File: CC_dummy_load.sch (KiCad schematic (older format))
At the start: 51 parts

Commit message: improvements
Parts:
- removed C? (x3): 100n, symbol C
- removed Q?: BUK954R8-60E, symbol Q_NMOS_GDS
- removed Q?: IRF540N, TO-220, symbol IRF540N
- added C? (x2): C, symbol C
- added C? (x3): 1uF, symbol CP
- added C? (x2): 100n, symbol C
- added C?: 10uF, symbol CP
- added Q?: IRF540N, TO-220, symbol IRF540N
- added Q?: Darl_NPN, symbol Darl_NPN
- added R?: 1k, symbol R
- R?: value R -> 1k
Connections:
- wire segments 148 -> 160
- no-connect marks 3 -> 4
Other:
- note added: "Set the POT\nat 9.k\n(div /10)"
- note removed: "Set the POT\nat 9.6k\n(div /10)"
- moved on the sheet: D?, P?, RV?, U?D

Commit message: final design v1
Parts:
- added D?: D, symbol D
- added P?: CONN_01X09, symbol CONN_01X09
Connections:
- net ARDU-P05 is gone; now on net ARDU-P09: R?.2
- net ARDU-A0: now also R?.2, TH?.1, P?.1 (P1); no longer R?.1, TH?.2
- net ARDU-P08: now also P?.3 (P3)
- net ARDU-P09: now also P?.4 (P4); no longer U?.2 (~CS~)
- net ARDU-P11: now also P?.5 (P5)
- net ARDU-P13: now also P?.7 (P7)
- net GND: now also TH?.2, P?.8 (P8); no longer R?.2
- net VCC: now also R?.1, D?.2 (A); no longer TH?.1
- net ARDU-P10 renamed ARDU-P12
- net ARDU-P12: now also P?.6 (P6)
- new net: D?.1 (K), P?.9 (P9)
- new net ARDU-P07: P?.2 (P2), U?.2 (~CS~)
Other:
- note added: "ARDU-GND"
- note added: "ARDU-Vin"
- moved on the sheet: R?, TH?

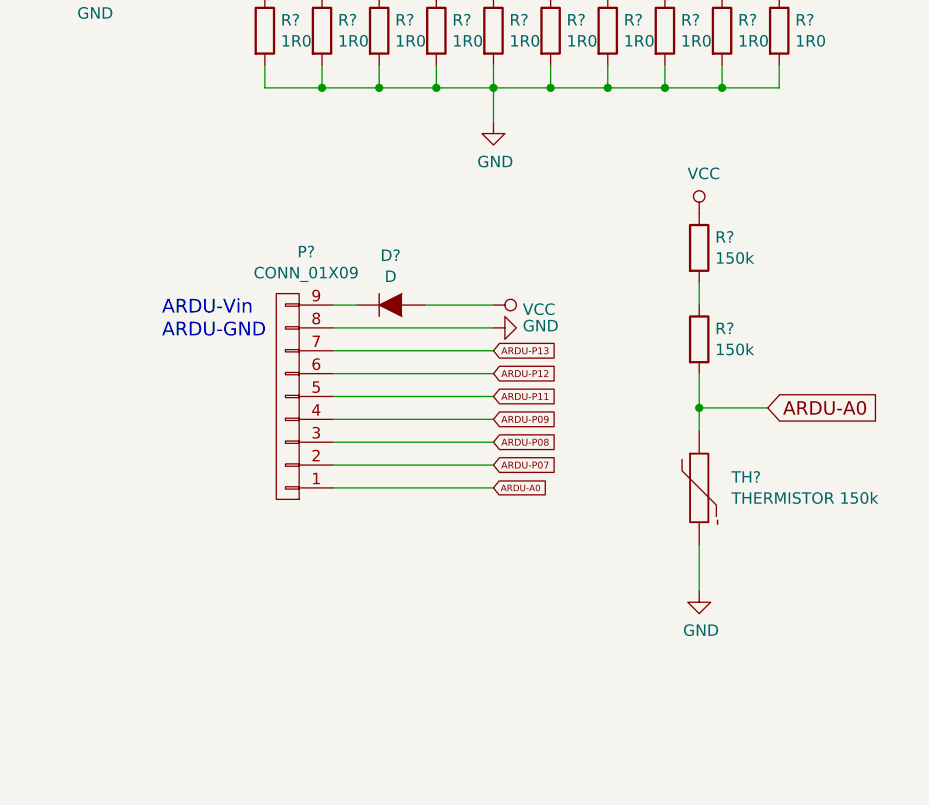
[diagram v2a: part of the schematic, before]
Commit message: change thermistor for LM35
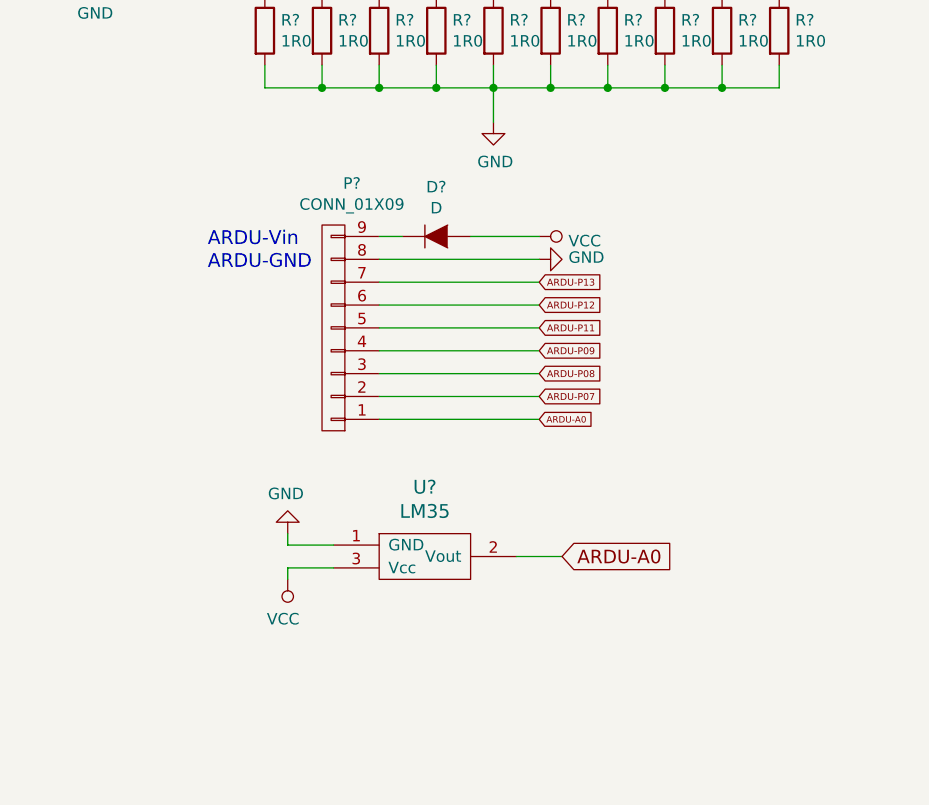
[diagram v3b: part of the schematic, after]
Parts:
- removed R? (x2): 150k, symbol R
- removed TH?: THERMISTOR 150k, symbol THERMISTOR
- added U?: LM35, symbol LM35
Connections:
- net ARDU-A0: now also U?.2 (Vout)
- net GND: now also U?.1 (GND)
- net VCC: now also U?.3 (Vcc)
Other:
- moved on the sheet: D?, P?
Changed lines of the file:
@@
 Connection ~ 6050 6450
-$Comp
-L THERMISTOR TH?
-U 1 1 56B01B45
-P 10350 5650
-F 0 "TH?" H 10491 5696 50  0000 L CNN
-F 1 "THERMISTOR 150k" H 10491 5604 50  0000 L CNN
-F 2 "" H 10350 5650 50  0000 C CNN
-F 3 "" H 10350 5650 50  0000 C CNN
-	1    10350 5650
-	1    0    0    -1
-$EndComp
 $Comp
 L VCC #PWR027
 U 1 1 56B01FB1
-P 10350 4450
-F 0 "#PWR027" H 10350 4300 50  0001 C CNN
-F 1 "VCC" H 10370 4624 50  0000 C CNN
-F 2 "" H 10350 4450 50  0000 C CNN
-F 3 "" H 10350 4450 50  0000 C CNN
-	1    10350 4450
-	1    0    0    -1
-$EndComp
-$Comp
-L R R?
-U 1 1 56B02027
-P 10350 4600
-F 0 "R?" H 10420 4646 50  0000 L CNN
-F 1 "150k" H 10420 4554 50  0000 L CNN
-F 2 "" V 10280 4600 50  0000 C CNN
-F 3 "" H 10350 4600 50  0000 C CNN
-	1    10350 4600
-	1    0    0    -1
+P 8550 6050
+F 0 "#PWR027" H 8550 5900 50  0001 C CNN
+F 1 "VCC" H 8570 6224 50  0000 C CNN
+F 2 "" H 8550 6050 50  0000 C CNN
+F 3 "" H 8550 6050 50  0000 C CNN
+	1    8550 6050
+	-1   0    0    1
 $EndComp
 $Comp
 L GND #PWR028
 U 1 1 56B020DD
-P 10350 6100
-F 0 "#PWR028" H 10350 5850 50  0001 C CNN
-F 1 "GND" H 10358 5926 50  0000 C CNN
-F 2 "" H 10350 6100 50  0000 C CNN
-F 3 "" H 10350 6100 50  0000 C CNN
-	1    10350 6100
-	1    0    0    -1
-$EndComp
-Text GLabel 10650 5300 2    59   Input ~ 0
+P 8550 5850
+F 0 "#PWR028" H 8550 5600 50  0001 C CNN
+F 1 "GND" H 8558 5676 50  0000 C CNN
+F 2 "" H 8550 5850 50  0000 C CNN
+F 3 "" H 8550 5850 50  0000 C CNN
+	1    8550 5850
+	-1   0    0    1
+$EndComp
+Text GLabel 9750 5950 2    59   Input ~ 0
 ARDU-A0
-$Comp
-L R R?
-U 1 1 56B025DE
-P 10350 5000
-F 0 "R?" H 10420 5046 50  0000 L CNN
-F 1 "150k" H 10420 4954 50  0000 L CNN
-F 2 "" V 10280 5000 50  0000 C CNN
-F 3 "" H 10350 5000 50  0000 C CNN
-	1    10350 5000
-	1    0    0    -1
-$EndComp
-Wire Wire Line
-	10350 4750 10350 4850
-Wire Wire Line
-	10350 5900 10350 6100
 $Comp
 L IRF540N Q?
@@
 	1    0    0    -1
 $EndComp
-Text GLabel 9450 5050 2    30   Input ~ 0
+Text GLabel 9650 4750 2    30   Input ~ 0
 ARDU-P13
-Text GLabel 9450 5150 2    30   Input ~ 0
+Text GLabel 9650 4850 2    30   Input ~ 0
 ARDU-P12
-Text GLabel 9450 5250 2    30   Input ~ 0
+Text GLabel 9650 4950 2    30   Input ~ 0
 ARDU-P11
-Text GLabel 9450 5450 2    30   Input ~ 0
+Text GLabel 9650 5150 2    30   Input ~ 0
 ARDU-P08
-Text GLabel 9450 5350 2    30   Input ~ 0
+Text GLabel 9650 5050 2    30   Input ~ 0
 ARDU-P09
 Wire Wire Line
-	9150 4850 9450 4850
-Wire Wire Line
-	8750 4950 9450 4950
-Wire Wire Line
-	8750 5050 9450 5050
-Wire Wire Line
-	8750 5150 9450 5150
-Wire Wire Line
-	8750 5250 9450 5250
-Wire Wire Line
-	8750 5350 9450 5350
-Wire Wire Line
-	8750 5450 9450 5450
+	9350 4550 9650 4550
+Wire Wire Line
+	8950 4650 9650 4650
+Wire Wire Line
+	8950 4750 9650 4750
+Wire Wire Line
+	8950 4850 9650 4850
+Wire Wire Line
+	8950 4950 9650 4950
+Wire Wire Line
+	8950 5050 9650 5050
+Wire Wire Line
+	8950 5150 9650 5150
 $Comp
 L D D?
 U 1 1 56C71A32
-P 9000 4850
-F 0 "D?" H 9000 5066 50  0000 C CNN
-F 1 "D" H 9000 4974 50  0000 C CNN
-F 2 "" H 9000 4850 50  0000 C CNN
-F 3 "" H 9000 4850 50  0000 C CNN
-	1    9000 4850
-	1    0    0    -1
-$EndComp
-Wire Wire Line
-	8850 4850 8750 4850
+P 9200 4550
+F 0 "D?" H 9200 4766 50  0000 C CNN
+F 1 "D" H 9200 4674 50  0000 C CNN
+F 2 "" H 9200 4550 50  0000 C CNN
+F 3 "" H 9200 4550 50  0000 C CNN
+	1    9200 4550
+	1    0    0    -1
+$EndComp
+Wire Wire Line
+	9050 4550 8950 4550
 $Comp
 L VCC #PWR?
 U 1 1 56C72879
-P 9450 4850
-F 0 "#PWR?" H 9450 4700 50  0001 C CNN
-F 1 "VCC" V 9470 4978 50  0000 L CNN
-F 2 "" H 9450 4850 50  0000 C CNN
-F 3 "" H 9450 4850 50  0000 C CNN
-	1    9450 4850
+P 9650 4550
+F 0 "#PWR?" H 9650 4400 50  0001 C CNN
+F 1 "VCC" V 9670 4678 50  0000 L CNN
+F 2 "" H 9650 4550 50  0000 C CNN
+F 3 "" H 9650 4550 50  0000 C CNN
+	1    9650 4550
 	0    1    1    0
 $EndComp
@@
 L GND #PWR?
 U 1 1 56C72A39
-P 9450 4950
-F 0 "#PWR?" H 9450 4700 50  0001 C CNN
-F 1 "GND" V 9458 4822 50  0000 R CNN
-F 2 "" H 9450 4950 50  0000 C CNN
-F 3 "" H 9450 4950 50  0000 C CNN
-	1    9450 4950
+P 9650 4650
+F 0 "#PWR?" H 9650 4400 50  0001 C CNN
+F 1 "GND" V 9658 4522 50  0000 R CNN
+F 2 "" H 9650 4650 50  0000 C CNN
+F 3 "" H 9650 4650 50  0000 C CNN
+	1    9650 4650
 	0    -1   -1   0
 $EndComp
-Text Notes 8000 4900 0    60   ~ 0
+Text Notes 8200 4600 0    60   ~ 0
 ARDU-Vin
-Text Notes 8000 5000 0    60   ~ 0
+Text Notes 8200 4700 0    60   ~ 0
 ARDU-GND
-Text GLabel 9450 5550 2    30   Input ~ 0
+Text GLabel 9650 5250 2    30   Input ~ 0
 ARDU-P07
-Text GLabel 9450 5650 2    28   Input ~ 0
+Text GLabel 9650 5350 2    28   Input ~ 0
 ARDU-A0
 $Comp
 L CONN_01X09 P?
 U 1 1 56C739E5
-P 8550 5250
-F 0 "P?" H 8469 4618 50  0000 C CNN
-F 1 "CONN_01X09" H 8469 4710 50  0000 C CNN
-F 2 "" H 8550 5250 50  0000 C CNN
-F 3 "" H 8550 5250 50  0000 C CNN
-	1    8550 5250
-	-1   0    0    1
-$EndComp
-Wire Wire Line
-	8750 5550 9450 5550
-Wire Wire Line
-	8750 5650 9450 5650
-Wire Wire Line
-	10350 5150 10350 5400
-Wire Wire Line
-	10650 5300 10350 5300
-Connection ~ 10350 5300
+P 8750 4950
+F 0 "P?" H 8669 4318 50  0000 C CNN
+F 1 "CONN_01X09" H 8669 4410 50  0000 C CNN
+F 2 "" H 8750 4950 50  0000 C CNN
+F 3 "" H 8750 4950 50  0000 C CNN
+	1    8750 4950
+	-1   0    0    1
+$EndComp
+Wire Wire Line
+	8950 5250 9650 5250
+Wire Wire Line
+	8950 5350 9650 5350
+$Comp
+L LM35 U?
+U 1 1 56C783B8
+P 9150 5950
+F 0 "U?" H 9150 6253 60  0000 C CNN
+F 1 "LM35" H 9150 6147 60  0000 C CNN
+F 2 "" H 9150 5950 60  0000 C CNN
+F 3 "" H 9150 5950 60  0000 C CNN
+	1    9150 5950
+	1    0    0    -1
+$EndComp
+Wire Wire Line
+	8550 5850 8550 5900
+Wire Wire Line
+	8550 5900 8750 5900
+Wire Wire Line
+	8550 6050 8550 6000
+Wire Wire Line
+	8550 6000 8750 6000
+Wire Wire Line
+	9550 5950 9750 5950
 $EndSCHEMATC

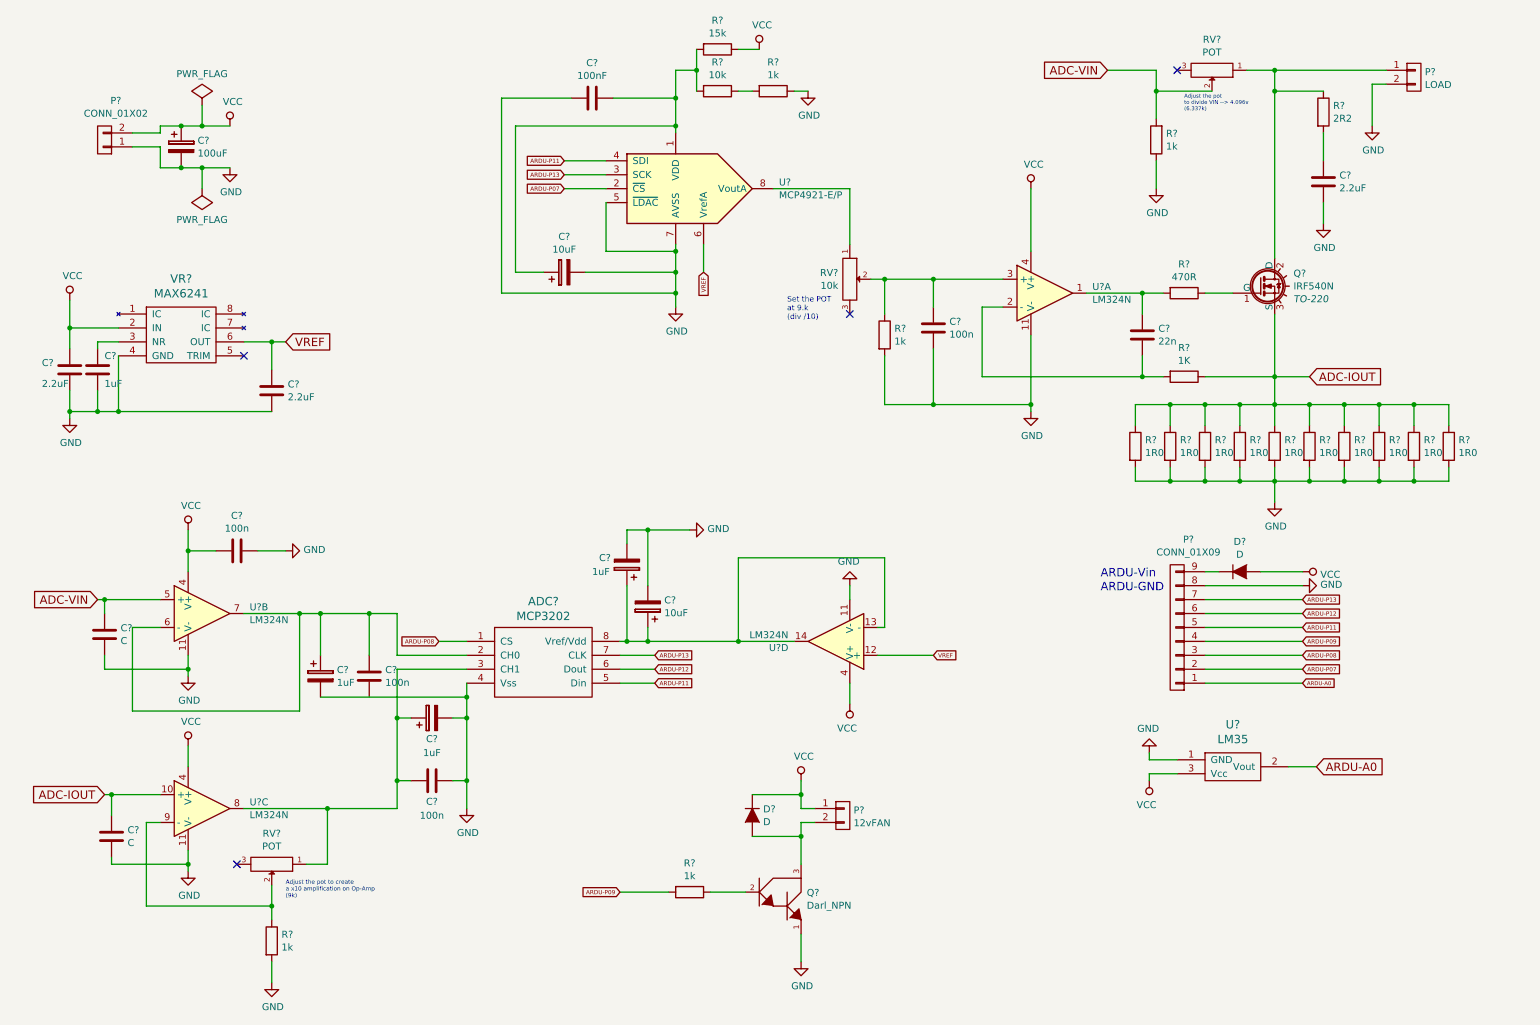
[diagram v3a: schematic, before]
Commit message: associated components and starting to layout PCB
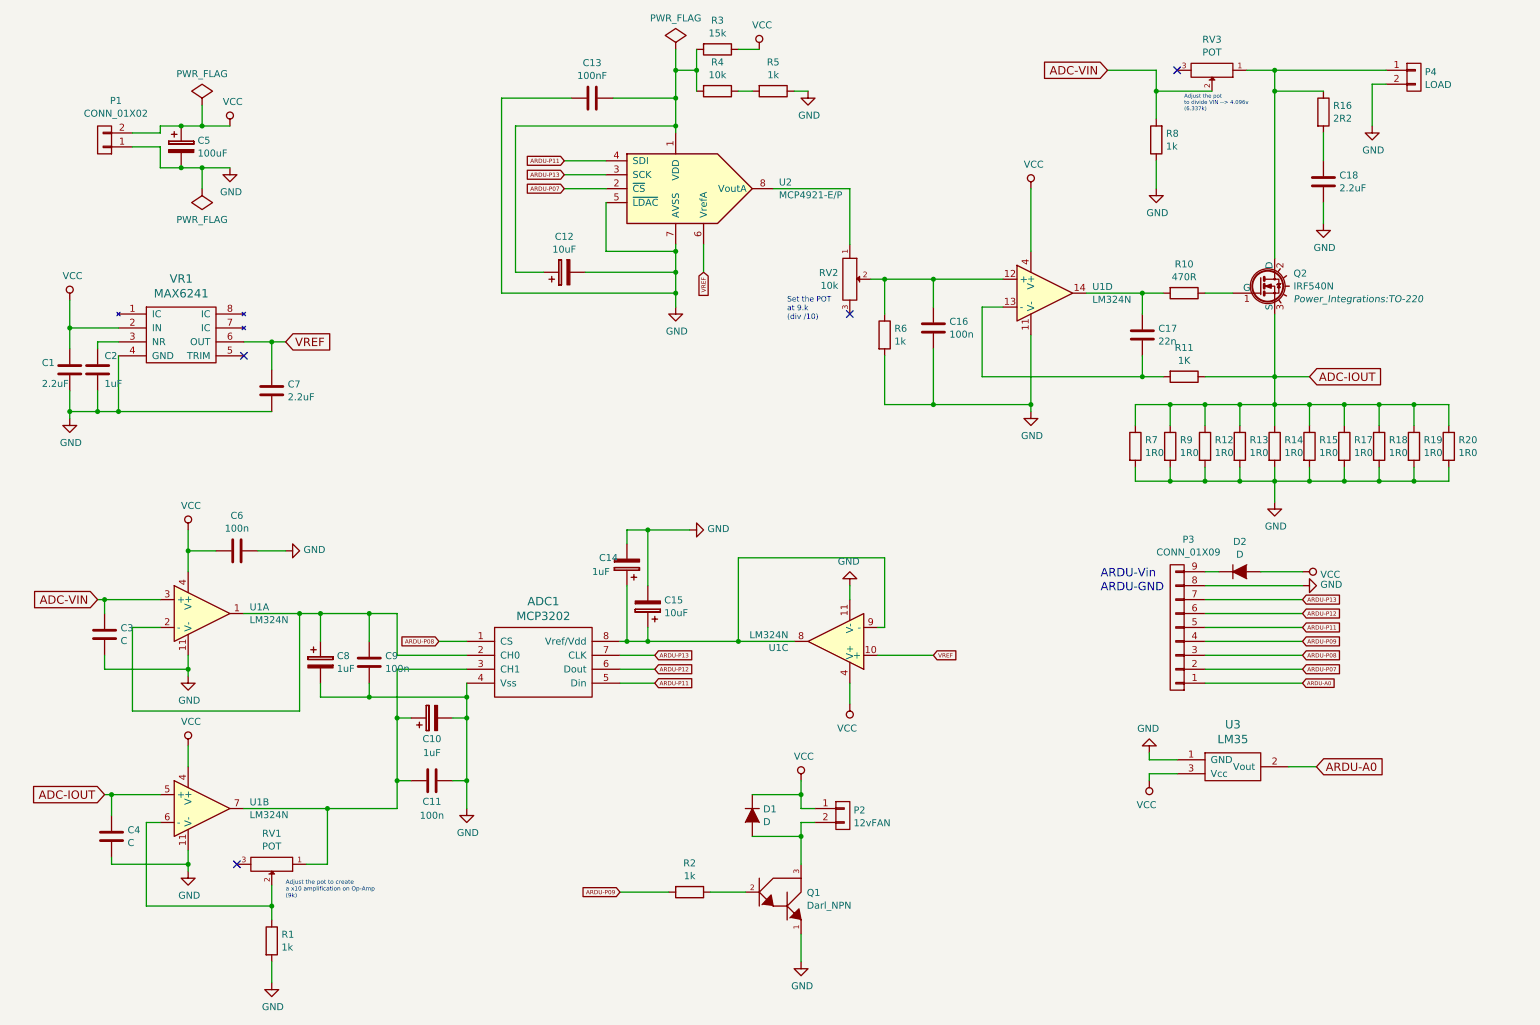
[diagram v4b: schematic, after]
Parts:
- ADC1: renamed from ADC?; footprint (none) -> Housings_DIP:DIP-8_W7.62mm
- C1, C11, C13, C16, C18, C7, C9: renamed from C?; footprint (none) -> Capacitors_ThroughHole:C_Disc_D6_P5
- C10, C12, C14, C15, C17, C2, C8: renamed from C?; footprint (none) -> Capacitors_ThroughHole:C_Radial_D5_L11_P2
- C3, C4, C6: renamed from C?; footprint (none) -> Capacitors_ThroughHole:C_Disc_D3_P2.5
- C5: renamed from C?; footprint (none) -> Capacitors_ThroughHole:C_Radial_D5_L11_P2.5
- D1, D2: renamed from D?; footprint (none) -> Diodes_ThroughHole:Diode_DO-41_SOD81_Horizontal_RM10
- P1, P2: renamed from P?; footprint (none) -> Pin_Headers:Pin_Header_Straight_1x02
- P3: renamed from P?; footprint (none) -> Pin_Headers:Pin_Header_Straight_1x09
- P4: renamed from P?; footprint (none) -> Connect:bornier2
- Q1: renamed from Q?; footprint (none) -> TO_SOT_Packages_THT:TO-92_Inline_Wide
- Q2: renamed from Q?; footprint TO-220 -> Power_Integrations:TO-220
- R1, R10, R11, R16, R2, R3, R4, R5, R6, R8: renamed from R?; footprint (none) -> Resistors_ThroughHole:Resistor_Horizontal_RM10mm
- R12, R13, R14, R15, R17, R18, R19, R20, R7, R9: renamed from R?; footprint (none) -> Resistors_ThroughHole:Resistor_Horizontal_RM20mm
- RV1, RV2, RV3: renamed from RV?; footprint (none) -> Potentiometers:Potentiometer_Trimmer-Suntan-TSR-3386P
- U1: renamed from U?; footprint (none) -> Housings_DIP:DIP-14_W7.62mm
- U2: renamed from U?; footprint (none) -> Housings_DIP:DIP-8_W7.62mm
- U3: renamed from U?; footprint (none) -> Pin_Headers:Pin_Header_Straight_1x03
- VR1: renamed from VR?; footprint (none) -> Housings_DIP:DIP-8_W7.62mm
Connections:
- net ADC-IOUT: now also U1.5 (+); no longer U1.10 (+)
- net ADC-VIN: now also U1.3 (+); no longer U1.5 (+)
- net GND: now also C9.2
- net VREF: now also U1.10 (+); no longer U1.12 (+)
- net at C17.1, R10.2: now also U1.14; no longer U1.1
- net at C17.2, R11.2: now also U1.13 (-); no longer U1.2 (-)
- net at C16.1, R6.1, RV2.2: now also U1.12 (+); no longer U1.3 (+)
- net at ADC1.2 (CH0), C8.1, C9.1: now also U1.1, U1.2 (-); no longer U1.6 (-), U1.7
- net at ADC1.3 (CH1), C10.1, C11.2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: now also U1.7; no longer U1.8
- net at R1.1, RV1.2: now also U1.6 (-); no longer U1.9 (-)
- net at ADC1.8 (Vref/Vdd), C14.1, C15.1: now also U1.8, U1.9 (-); no longer U1.13 (-), U1.14
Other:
- moved on the sheet: C8, C9
